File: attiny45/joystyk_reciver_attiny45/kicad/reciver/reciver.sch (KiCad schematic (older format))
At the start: 14 parts, among them J1 DRIVES, J2 XY-MK-5V, J3 PWR, U1 ATtiny45-20PU, U2 L7805, U3 LM317_3PinPackage

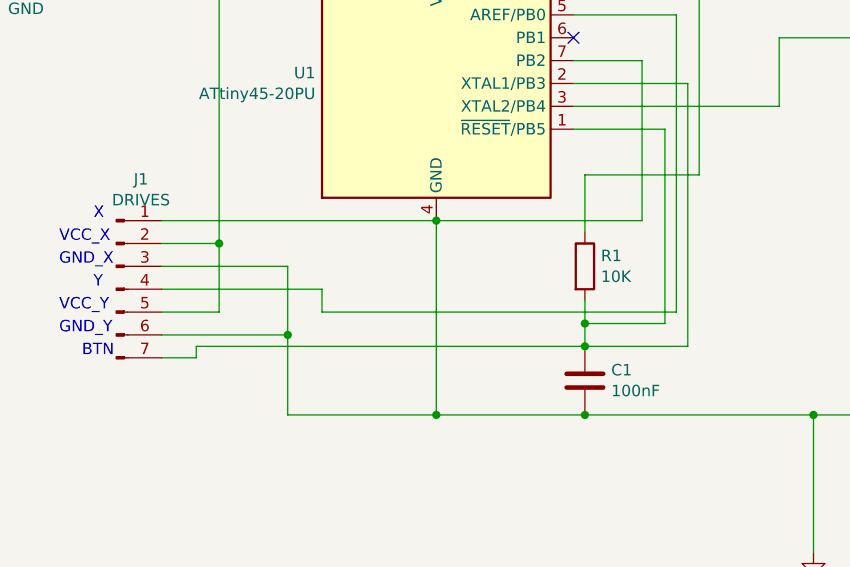
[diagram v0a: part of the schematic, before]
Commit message: Added fix to the reciever kicad schema
Signed-off-by: Alexey B <bayrepo.info@gmail.com>
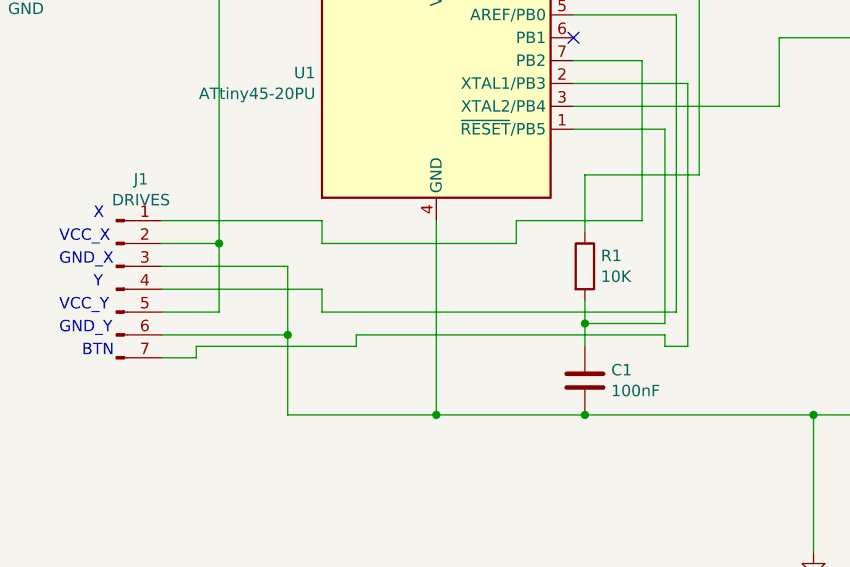
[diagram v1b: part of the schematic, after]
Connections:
- net GND: no longer J1.1 (Pin_1), U1.7 (PB2)
- net at C1.1, R1.2, U1.1 (~RESET~/PB5): no longer J1.7 (Pin_7), U1.2 (XTAL1/PB3)
- new net: J1.7 (Pin_7), U1.2 (XTAL1/PB3)
- new net: J1.1 (Pin_1), U1.7 (PB2)
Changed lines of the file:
@@
 	5300 4150 5300 5300
-Wire Wire Line
-	5300 5300 4850 5300
 Wire Wire Line
 	3150 5300 3150 5350
 Wire Wire Line
 	3150 5350 3000 5350
-Connection ~ 4850 5300
-Wire Wire Line
-	4850 5300 3150 5300
 Wire Wire Line
 	4200 5600 3550 5600
@@
 Wire Wire Line
 	5100 4050 5100 4750
-Wire Wire Line
-	5100 4750 4200 4750
-Connection ~ 4200 4750
-Wire Wire Line
-	4200 4750 3000 4750
 Wire Wire Line
 	5250 3850 5250 5150
@@
 Wire Wire Line
 	2400 3650 2400 3450
+Wire Wire Line
+	5100 4750 4550 4750
+Wire Wire Line
+	4550 4750 4550 4850
+Wire Wire Line
+	4550 4850 3700 4850
+Wire Wire Line
+	3700 4850 3700 4750
+Wire Wire Line
+	3700 4750 3000 4750
+Wire Wire Line
+	5300 5300 5200 5300
+Wire Wire Line
+	5200 5300 5200 5250
+Wire Wire Line
+	5200 5250 3850 5250
+Wire Wire Line
+	3850 5250 3850 5300
+Wire Wire Line
+	3850 5300 3150 5300
 $EndSCHEMATC

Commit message: Added renew recv kicad scheme
Signed-off-by: Alexey B <bayrepo.info@gmail.com>
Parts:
- added D1: LED, transmitter:R_my_5_08, symbol Device:LED
- added R6: 220, transmitter:R_my_5_08, symbol Device:R
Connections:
- net GND: now also R6.2
- net at J1.7 (Pin_7), U1.2 (XTAL1/PB3): now also D1.2 (A)
- new net: D1.1 (K), R6.1
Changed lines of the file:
@@
 	3850 5250 3850 5300
 Wire Wire Line
-	3850 5300 3150 5300
+	3850 5300 3300 5300
+$Comp
+L Device:LED D1
+U 1 1 5E1F5D0B
+P 3300 5900
+F 0 "D1" V 3339 5783 50  0000 R CNN
+F 1 "LED" V 3248 5783 50  0000 R CNN
+F 2 "transmitter:R_my_5_08" H 3300 5900 50  0001 C CNN
+F 3 "~" H 3300 5900 50  0001 C CNN
+	1    3300 5900
+	0    -1   -1   0
+$EndComp
+$Comp
+L Device:R R6
+U 1 1 5E1FE7AA
+P 3300 6350
+F 0 "R6" H 3370 6396 50  0000 L CNN
+F 1 "220" H 3370 6305 50  0000 L CNN
+F 2 "transmitter:R_my_5_08" V 3230 6350 50  0001 C CNN
+F 3 "~" H 3300 6350 50  0001 C CNN
+	1    3300 6350
+	1    0    0    -1
+$EndComp
+$Comp
+L power:GND #PWR0103
+U 1 1 5E1FF23C
+P 3300 6700
+F 0 "#PWR0103" H 3300 6450 50  0001 C CNN
+F 1 "GND" H 3305 6527 50  0000 C CNN
+F 2 "" H 3300 6700 50  0001 C CNN
+F 3 "" H 3300 6700 50  0001 C CNN
+	1    3300 6700
+	1    0    0    -1
+$EndComp
+Wire Wire Line
+	3300 6700 3300 6500
+Wire Wire Line
+	3300 6200 3300 6050
+Wire Wire Line
+	3300 5750 3300 5300
+Connection ~ 3300 5300
+Wire Wire Line
+	3300 5300 3150 5300
 $EndSCHEMATC
